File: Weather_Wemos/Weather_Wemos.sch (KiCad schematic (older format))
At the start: 21 parts, among them J1 Pwr In, J2 12V, J3 Rain Adv, J4 WIND, J5 RAIN, J6 Rain Serial, J7 Exp, U1 WeMos_D1_mini, U2 L7805

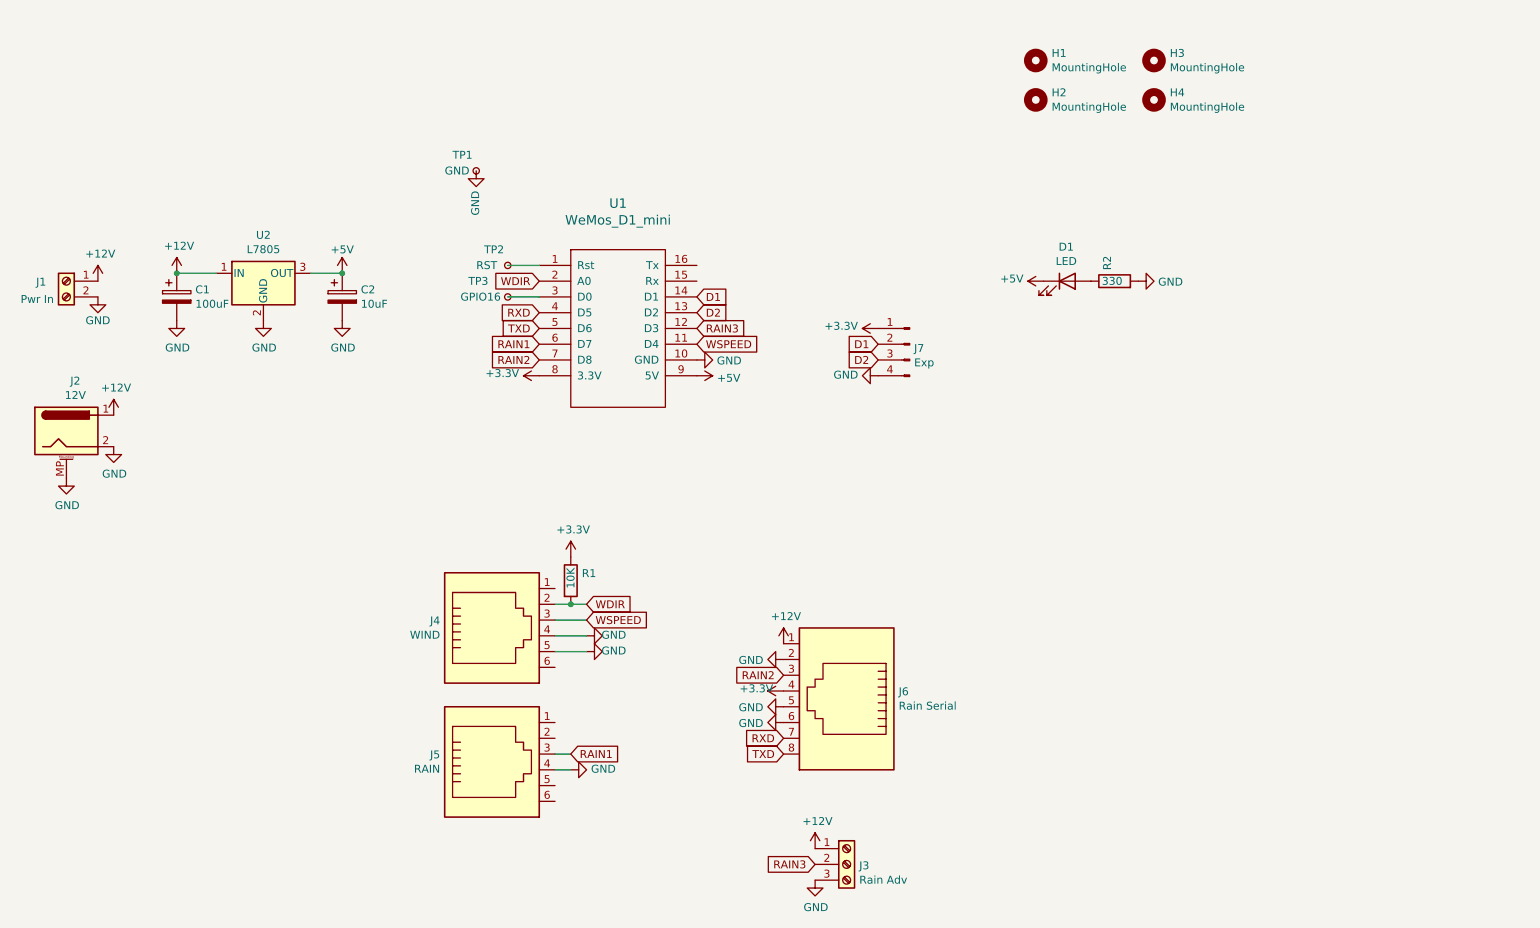
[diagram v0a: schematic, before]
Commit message: added PDF schematic and Updated Project name in files
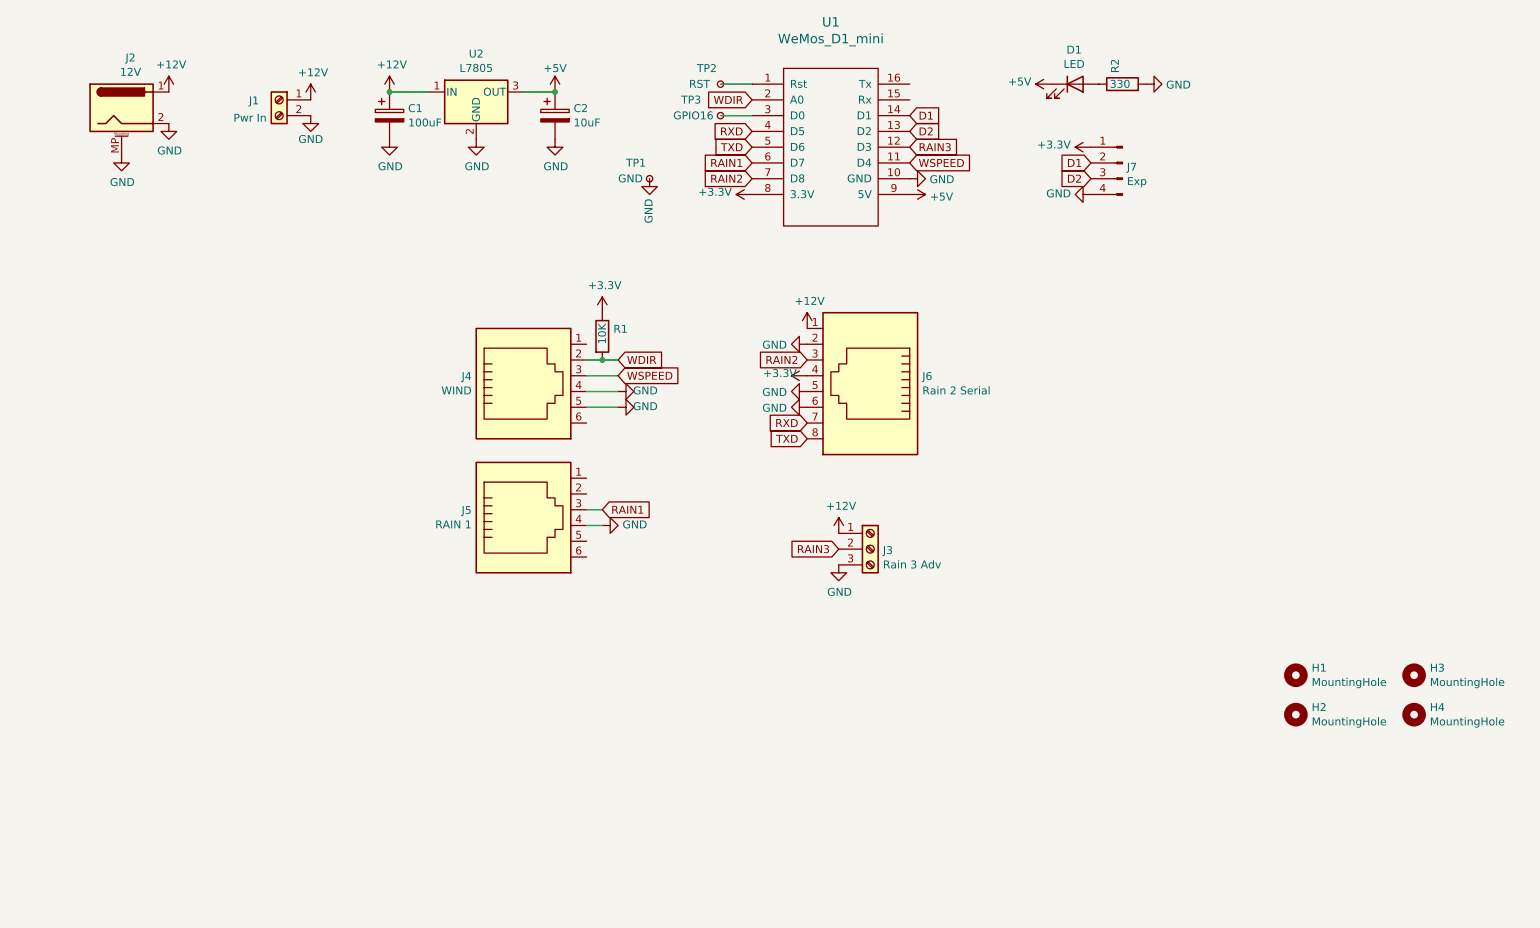
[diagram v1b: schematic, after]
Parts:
- J3: value Rain Adv -> Rain 3 Adv
- J5: value RAIN -> RAIN 1
- J6: value Rain Serial -> Rain 2 Serial
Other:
- moved on the sheet: C1, C2, D1, H1, H2, H3, H4, J1, J2, J3, J4, J5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
